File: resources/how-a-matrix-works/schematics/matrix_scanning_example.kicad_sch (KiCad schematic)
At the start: 32 parts

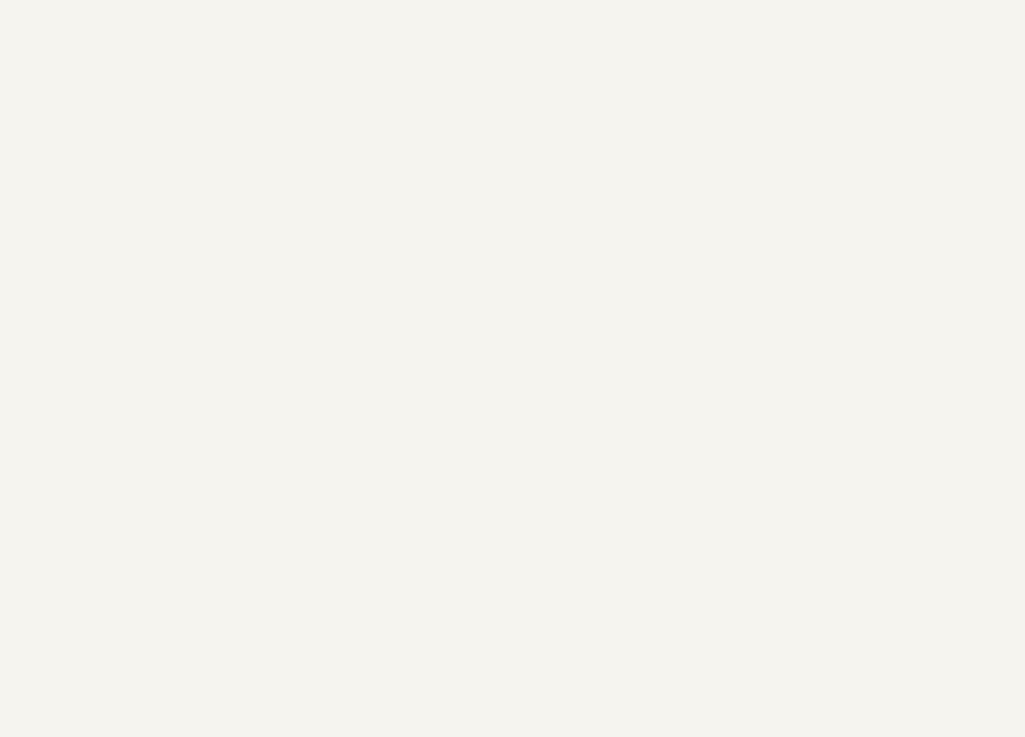
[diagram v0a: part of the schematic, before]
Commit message: add initial step for matrix scan
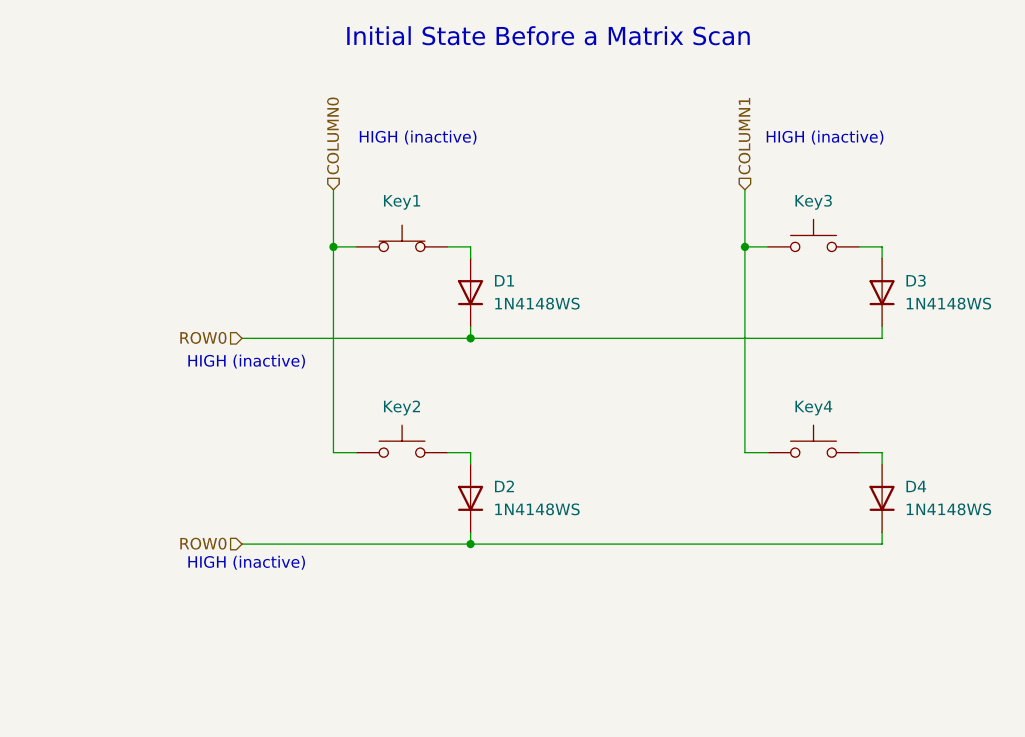
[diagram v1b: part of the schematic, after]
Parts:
- added D1, D2, D3, D4: 1N4148WS, Custom:1N4148WS_SOD-323, symbol Diode:1N4148WS
- added Key1, Key3, Key4: ~, Custom:1u_Cherry_MX1A_5Pin_Switch_Kailh_Socket_with_SK6812MINI-E_cutout, symbol Switch:SW_Push
- added Key2: ~, Custom:1u_Cherry_MX1A_5Pin_Switch_Kailh_Socket_with_SK6812MINI-E_cutout, symbol custom:1u_Cherry_MX_Switch_RGB-SK6812MINI-E_cutout
- Key1, Key2, Key3, Key4: value (none) -> ~
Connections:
- net COLUMN0: now also Key1.1, Key2.1
- net COLUMN1: now also Key3.1, Key4.1
- net ROW0: now also D1.1 (K), D2.1 (K), D3.1 (K), D4.1 (K)
- new net: D3.2 (A), Key3.2
- new net: D4.2 (A), Key4.2
- new net: D2.2 (A), Key2.2
- new net: D1.2 (A), Key1.2
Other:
- note added: "Initial State Before a Matrix Scan"
